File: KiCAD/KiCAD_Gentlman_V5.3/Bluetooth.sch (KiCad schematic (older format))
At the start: 26 parts, among them J7 PinHeader2.54mm_5, U7 nRF52832-QFAA, U8 nRF52832_DM-SModule, U9 nRF52810_PLE52M, Y1 Y_32MHz

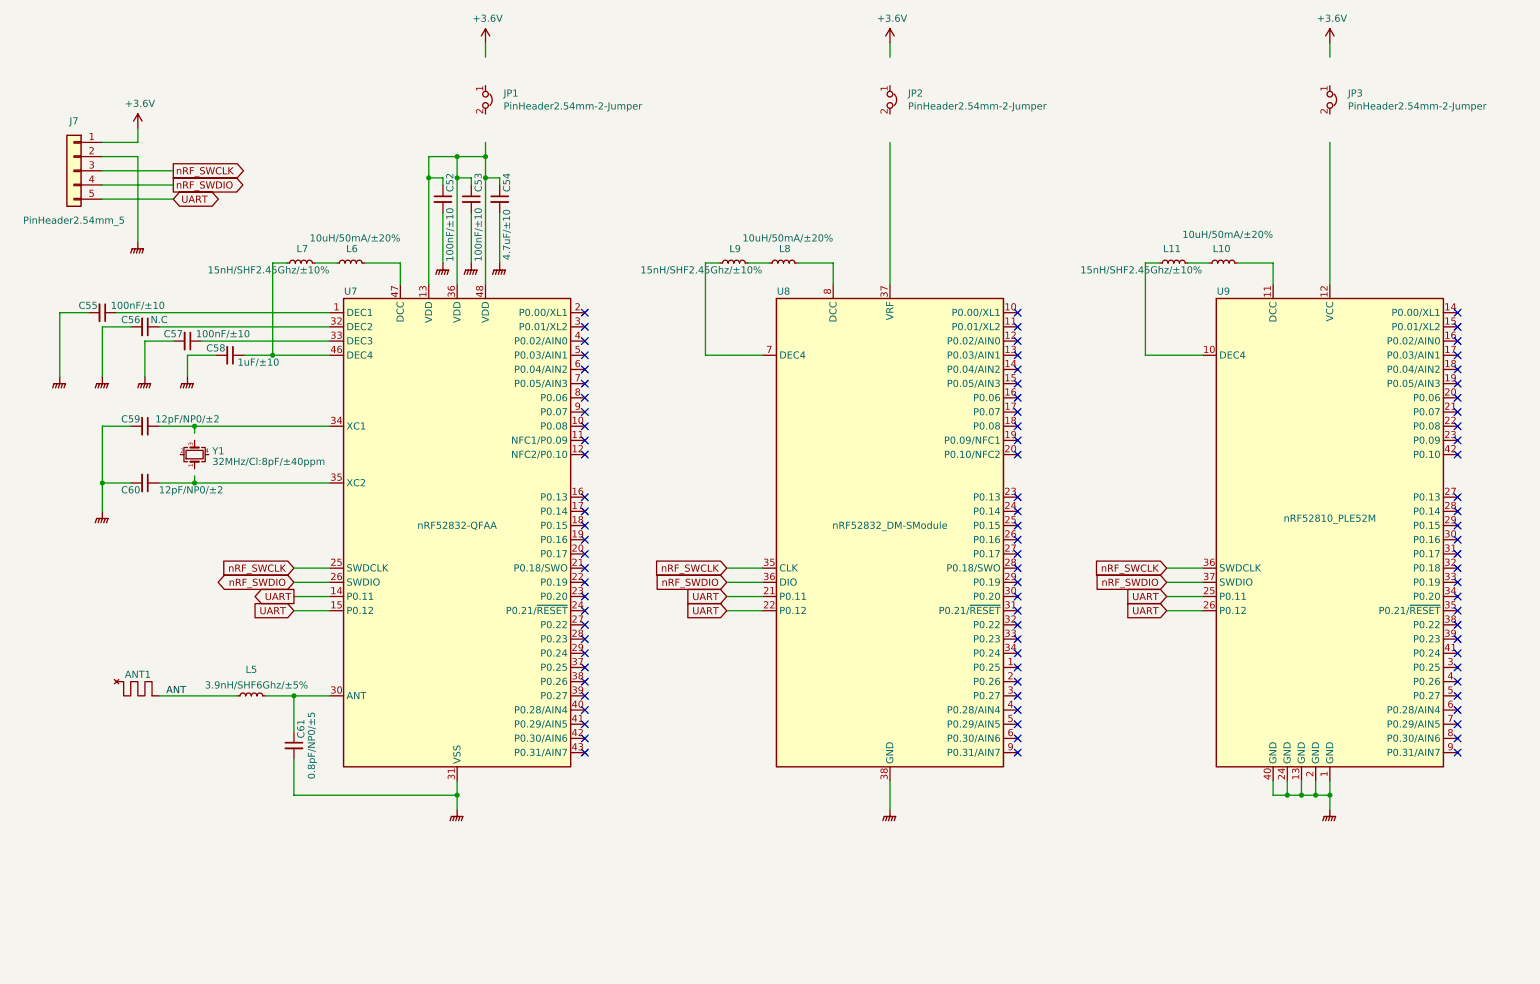
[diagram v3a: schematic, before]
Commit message: KSG : 보드 수정(크리스탈 배치 문제, 점퍼추가, 이름위치오기수정, IC1번핀표시)
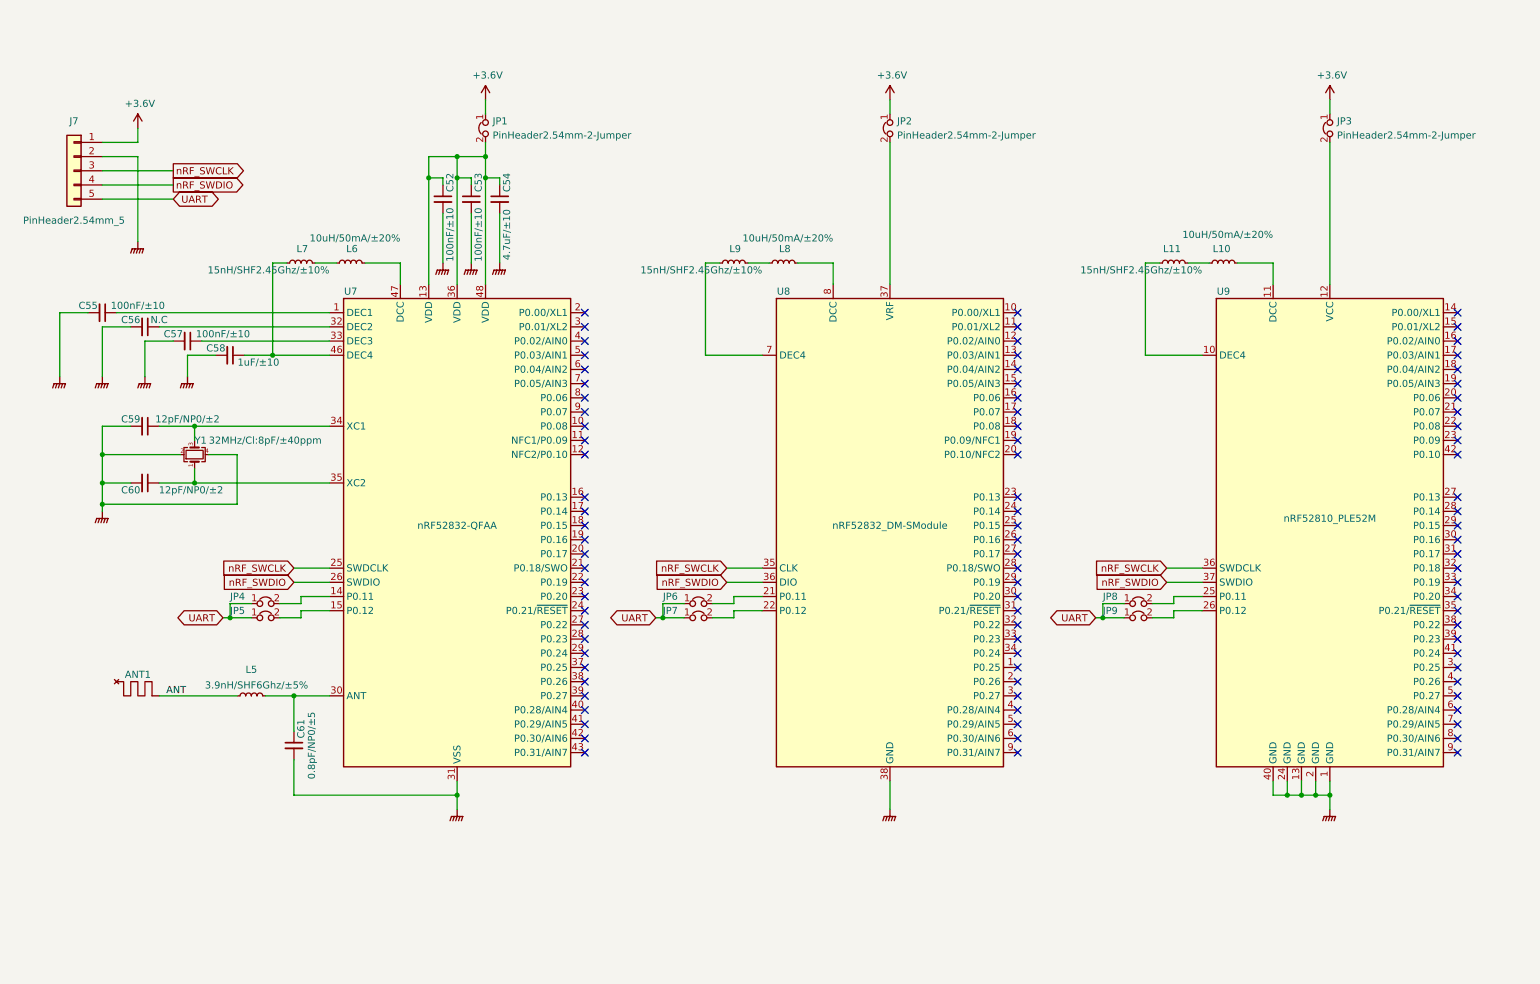
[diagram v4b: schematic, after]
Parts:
- added JP4, JP5, JP6, JP7, JP8, JP9: PinHeader2.54mm-2-Jumper, Custom:PinHeader_1x02_P2.54mm_Vertical, symbol Custom:PinHeader2.54mm-2-Jumper
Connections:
- wire segments 101 -> 131
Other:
- moved on the sheet: JP1, JP2, JP3
